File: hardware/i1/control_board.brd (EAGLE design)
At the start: 151 x 68.3 mm, 47 parts, among them IC1 4021N, J1 AUDIO_JACK_3.5MM_KIT, P2 PTV112-4420A-A503

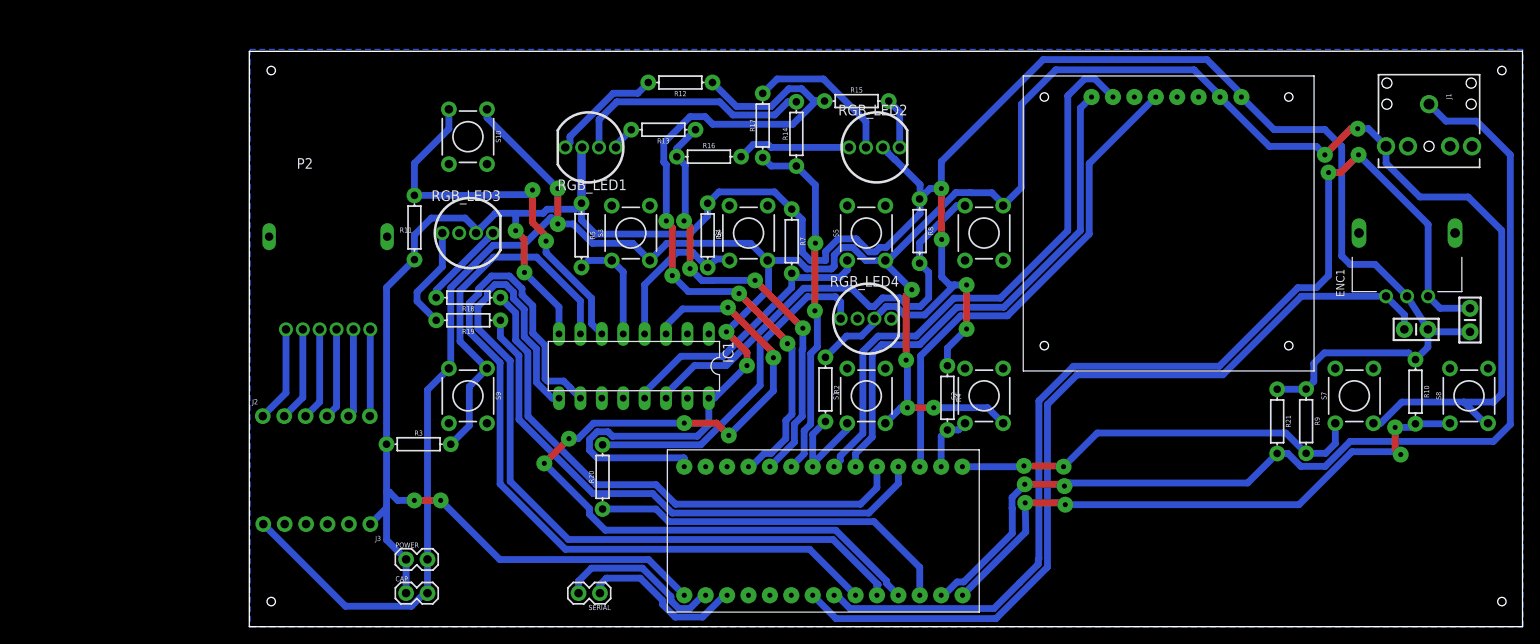
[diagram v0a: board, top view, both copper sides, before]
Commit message: Re-space controls - add mounting holes for RPi
Add audio hat
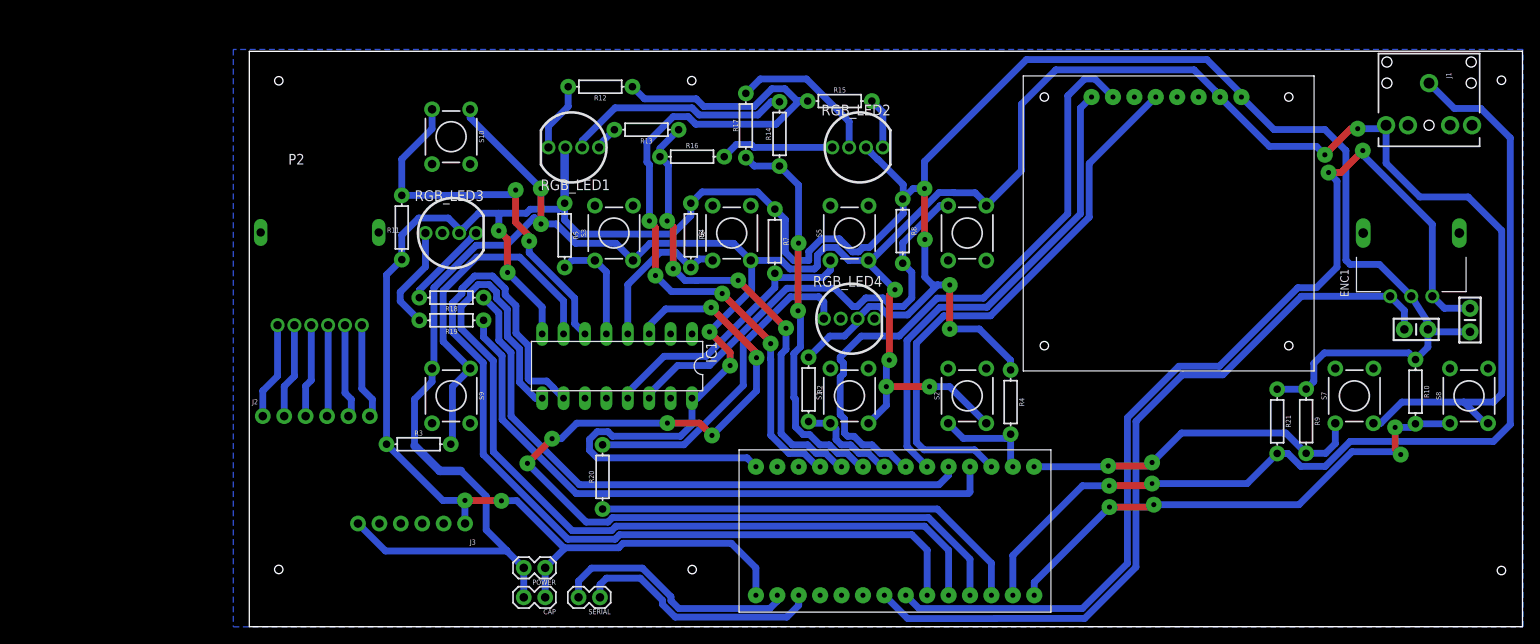
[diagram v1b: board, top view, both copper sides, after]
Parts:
- moved POWER 16.5 mm to (63.5, 6.00), turned to 180 degrees
- moved CAP 16.5 mm to (63.5, 2.50), turned to 180 degrees
- moved J3 11.2 mm to (54.0, 11.3)
- moved R12 9.51 mm to (70.0, 63.1)
- moved U$1 8.50 mm to (86.5, 20.0)
- moved R4 7.52 mm to (118.7, 25.7)
- moved J1 2.50 mm to (168.4, 63.5)
- moved IC1 2.00 mm to (72.0, 29.9)
- moved R13 2.00 mm to (75.5, 58.0)
- moved R14 2.00 mm to (91.3, 57.5)
- moved R15 2.00 mm to (98.5, 61.4)
- moved R16 2.00 mm to (80.9, 54.8)
- moved R17 2.00 mm to (87.3, 58.5)
- moved R18 2.00 mm to (52.4, 38.1)
- moved R19 2.00 mm to (52.4, 35.4)
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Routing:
- net N$1: track 102.4 -> 115.2 mm
- net N$4: track 96.2 -> 108.2 mm
- net 3.3V: track 370.5 -> 382.0 mm
- net N$8: track 93.7 -> 104.7 mm
- net N$18: track 71.6 -> 61.8 mm
- net N$17: track 19.7 -> 29.4 mm
- net N$28: track 20.1 -> 29.5 mm
- net N$19: track 101.1 -> 91.8 mm
- net WB_LED_G: track 65.7 -> 74.9 mm
- net PL_LED_G: track 43.8 -> 52.6 mm
- net N$11: track 49.8 -> 41.5 mm
- net N$20: track 129.4 -> 121.3 mm
- net ZN_LED_R: track 89.1 -> 97.1 mm
- net WB_LED_R: track 64.5 -> 72.2 mm
- net GND: track 363.8 -> 371.2 mm
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
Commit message: Add wristband schematic and board layout
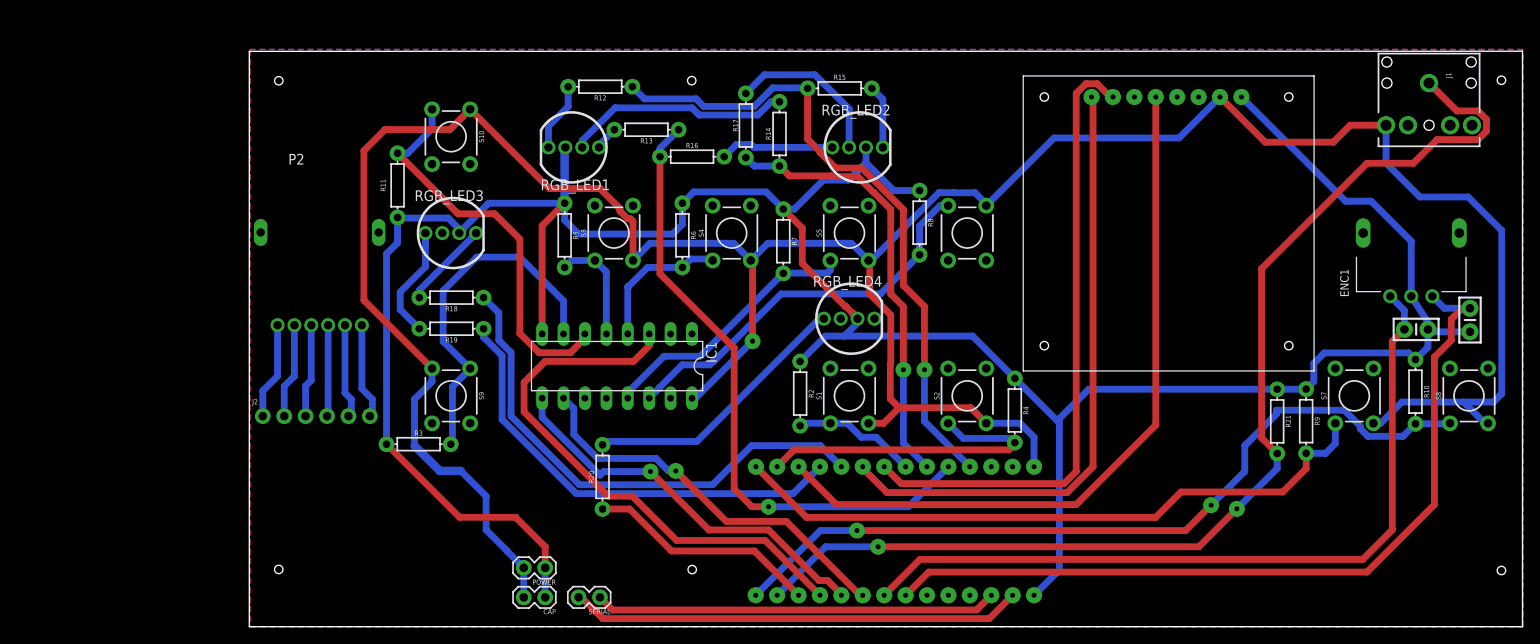
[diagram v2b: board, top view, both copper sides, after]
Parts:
- removed J3: (no value), SparkFun-Connectors:1X06_NO_SILK
- moved U$1 37.0 mm to (123.5, 20.0), flipped to the bottom
- moved R11 5.02 mm to (46.0, 51.4)
- moved R8 2.24 mm to (107.9, 47.0)
- moved R15 1.50 mm to (98.5, 62.9)
- moved R2 1.12 mm to (93.8, 26.7)
- moved R4 1.12 mm to (119.2, 24.7)
- moved R19 1.00 mm to (52.4, 34.4)
- moved R6 1.00 mm to (79.8, 45.5)
- moved R7 1.00 mm to (91.8, 44.8)
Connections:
- net 3.3V: no longer J3.6
- net GND: no longer J3.1
- net N$19: now also U$1.6; no longer U$1.5
- net N$20: now also U$1.5; no longer U$1.6
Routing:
- net N$4: track 108.2 -> 47.0 mm, vias 0 -> 1
- net N$8: track 104.7 -> 46.9 mm, vias 0 -> 1
- net N$1: track 115.2 -> 65.7 mm, vias 6 -> 0
- net 3.3V: track 382.0 -> 339.0 mm, vias 10 -> 1
- net GND: track 371.2 -> 330.3 mm, vias 8 -> 0
- net N$11: track 41.5 -> 78.3 mm, vias 2 -> 0
- net N$18: track 61.8 -> 95.6 mm, vias 4 -> 2
- net N$10: track 12.3 -> 38.3 mm
- net PL_LED_G: track 52.6 -> 27.5 mm
- net N$28: track 29.5 -> 53.7 mm
- net N$20: track 121.3 -> 97.8 mm, vias 2 -> 0
- net N$31: track 66.1 -> 87.1 mm
- net WB_LED_G: track 74.9 -> 54.3 mm
- net ZN_LED_R: track 97.1 -> 77.4 mm, vias 4 -> 1
- net ZN_LED_G: track 56.0 -> 75.4 mm, vias 4 -> 1
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- added copper zone on layer 1, net GND

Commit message: Change pad size of LEDs
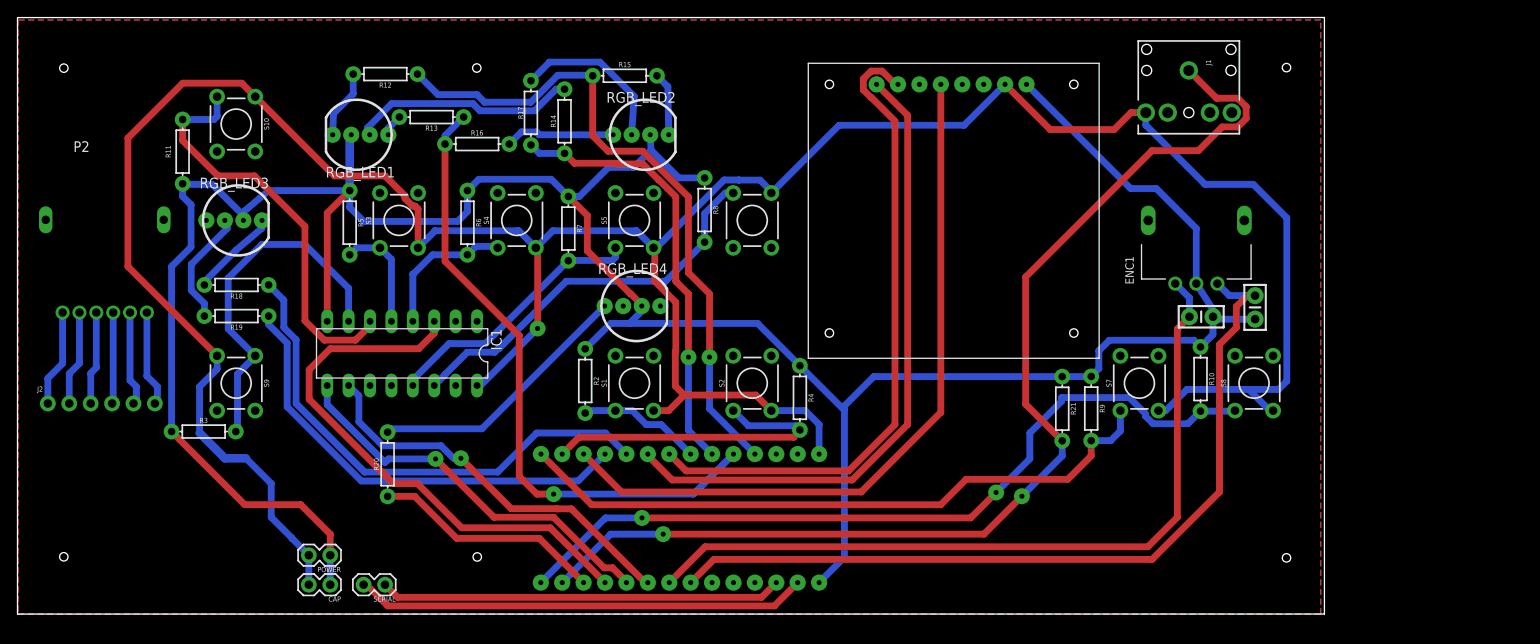
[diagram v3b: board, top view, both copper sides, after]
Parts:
- moved J1 28.5 mm to (139.9, 65.0)
- moved R11 25.8 mm to (20.5, 55.4)
- moved R21 25.5 mm to (124.8, 24.9)
- moved R12 25.5 mm to (44.5, 64.6)
- moved R16 25.5 mm to (55.4, 56.3)
- moved R18 25.5 mm to (26.9, 39.6)
- moved R19 25.5 mm to (26.9, 35.9)
- moved R3 25.5 mm to (23.0, 22.2)
- moved S10 25.5 mm to (26.8, 58.6)
- moved S9 25.5 mm to (26.8, 27.9)
- moved C3 25.5 mm to (141.3, 35.8)
- moved C4 25.5 mm to (147.7, 36.9)
- moved CAP 25.5 mm to (38.0, 4.00)
- moved ENC1 25.5 mm to (140.8, 47.2)
- moved IC1 25.5 mm to (46.5, 31.4)
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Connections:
- net N$24: now also RGB_LED3.B; no longer RGB_LED3.G
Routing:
- net GND: track 330.3 -> 335.2 mm
- net 3.3V: track 339.0 -> 342.1 mm
- net N$30: track 74.5 -> 77.6 mm
- net N$9: track 73.9 -> 76.8 mm
- net N$22: track 47.4 -> 48.9 mm
- net ZN_LED_R: track 77.4 -> 78.8 mm
- net N$14: track 133.4 -> 132.5 mm
- net N$6: track 13.6 -> 13.1 mm
- net N$26: track 32.4 -> 31.9 mm
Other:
- board size 151 x 68.3 mm -> 155 x 70.8 mm
